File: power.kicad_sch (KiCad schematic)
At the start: 22 parts, among them U19 AP62301_TSOT, U20 AP62301_TSOT

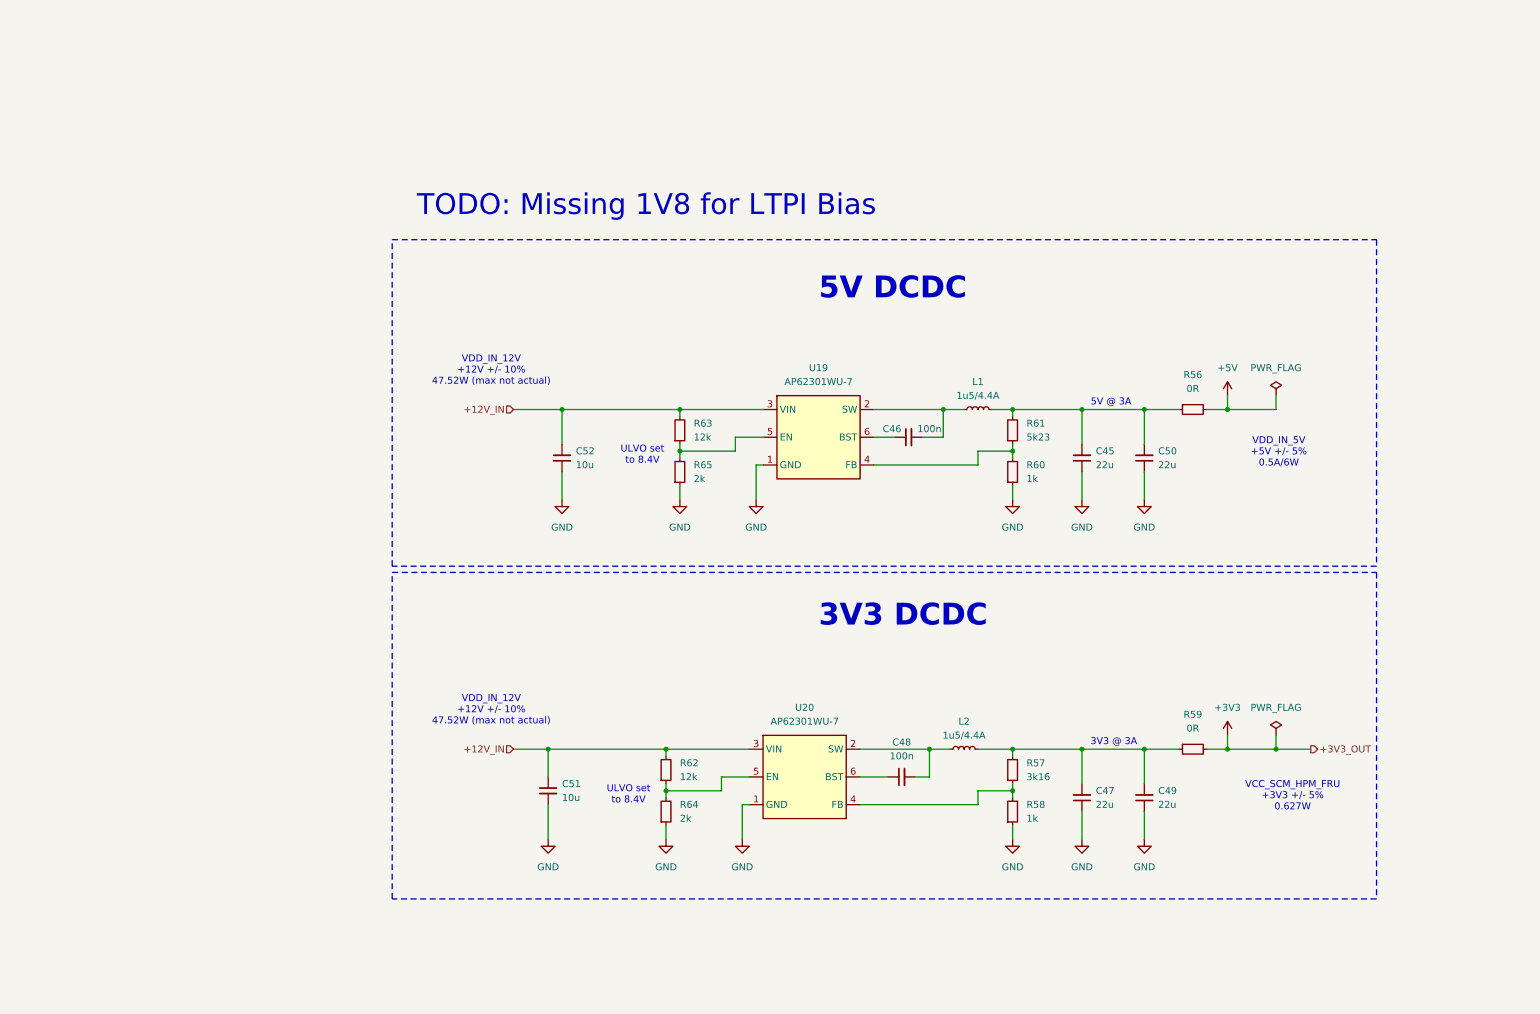
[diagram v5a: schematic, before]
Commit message: [#83363] Replaced 1V8 LDO with DC/DC and moved it to power sheet
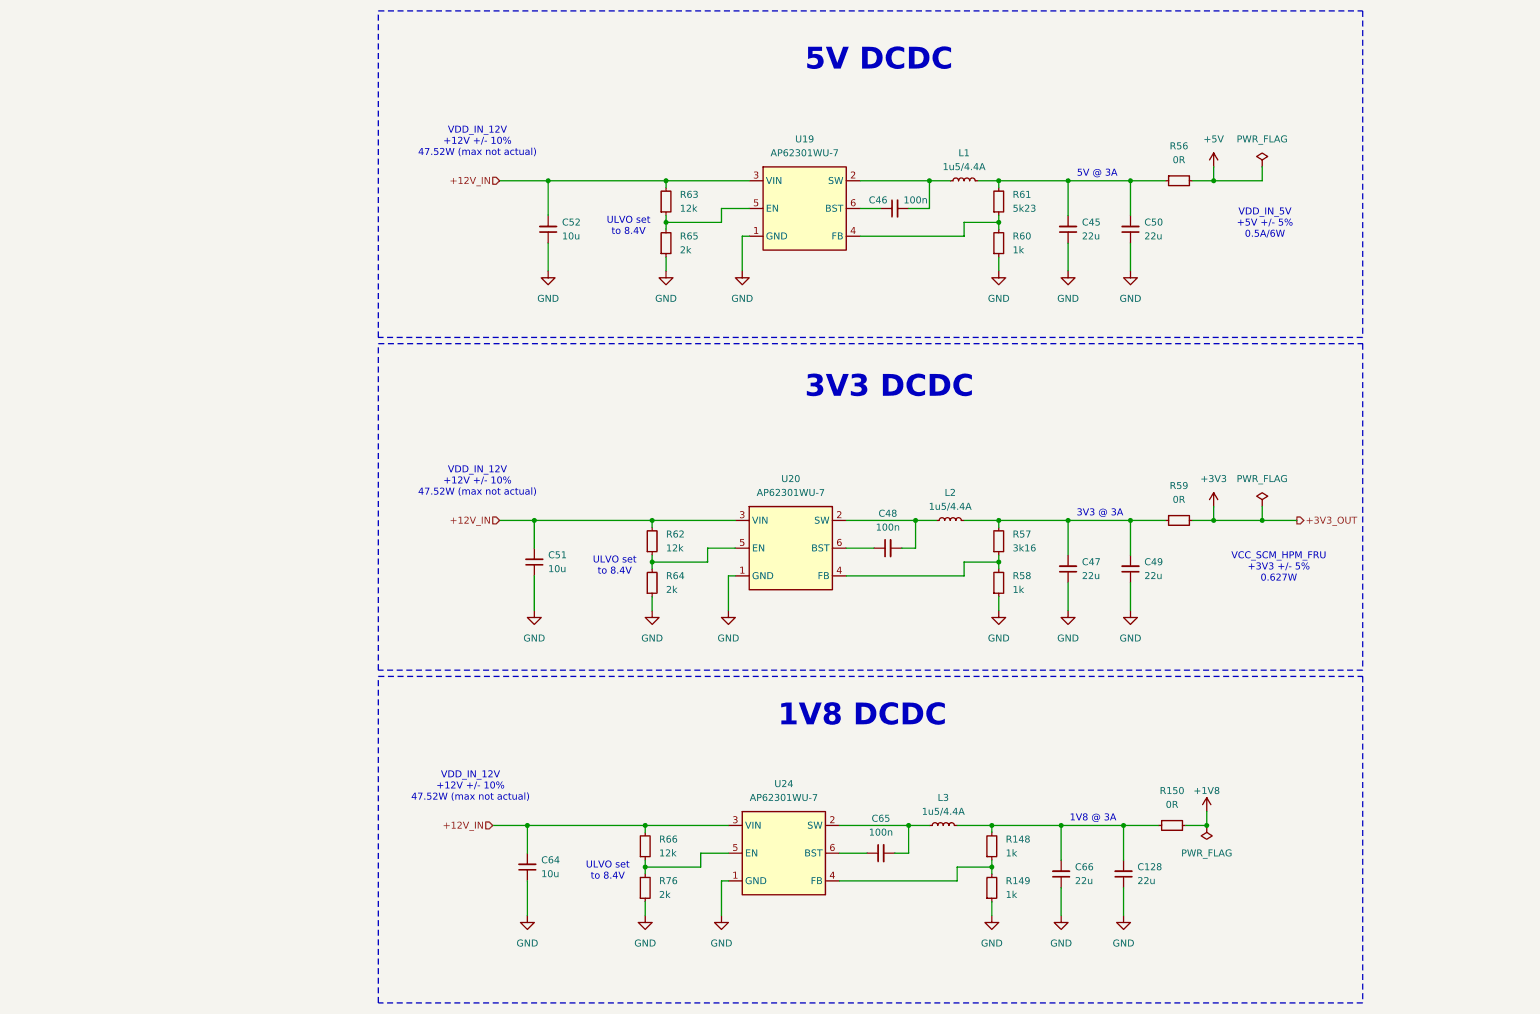
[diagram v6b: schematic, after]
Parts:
- added C128, C66: C_22u_0805_16V, antmicro-footprints:C_0805_2012Metric, symbol antmicroCapacitorsmisc:C_22u_0805_16V
- added C64: C_10u_25V_0603, antmicro-footprints:C_0603_1608Metric, symbol antmicroCapacitors0603:C_10u_25V_0603
- added C65: C_100n_0402, antmicro-footprints:C_0402_1005Metric, symbol antmicroCapacitors0402:C_100n_0402
- added L3: L_1u5_4.4A_Bourns-SRP3212A, antmicro-footprints:L_Bourns-SRP3212A, symbol antmicroFixedInductors:L_1u5_4.4A_Bourns-SRP3212A
- added R148, R149: R_1k_0402, antmicro-footprints:R_0402_1005Metric, symbol antmicroResistors0402:R_1k_0402
- added R150: R_0R_0402, antmicro-footprints:R_0402_1005Metric, symbol antmicroResistors0402:R_0R_0402
- added R66: R_12k_0402, antmicro-footprints:R_0402_1005Metric, symbol antmicroResistors0402:R_12k_0402
- added R76: R_2k_0402, antmicro-footprints:R_0402_1005Metric, symbol antmicroResistors0402:R_2k_0402
- added U24: AP62301_TSOT, antmicro-footprints:TSOT23-6, symbol antmicroDCDCConverters:AP62301_TSOT
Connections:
- net +12V_IN: now also C64.2, R66.2, U24.3 (VIN)
- net GND: now also C128.1, C64.1, C66.1, R149.1, R76.1, U24.1 (GND)
- new net: C65.1, U24.6 (BST)
- new net: C65.2, L3.1, U24.2 (SW)
- new net: R148.1, R149.2, U24.4 (FB)
- new net: R66.1, R76.2, U24.5 (EN)
- new net: C128.2, C66.2, L3.2, R148.2, R150.1
- new net +1V8: R150.2
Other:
- note added: "1V8 @ 3A"
- note added: "1V8 DCDC"
- note removed: "TODO: Missing 1V8 for LTPI Bias"
- moved on the sheet: C45, C46, C47, C48, C49, C50, C51, C52, L1, L2, R56, R57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

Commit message: [#83609] Add load switch IC
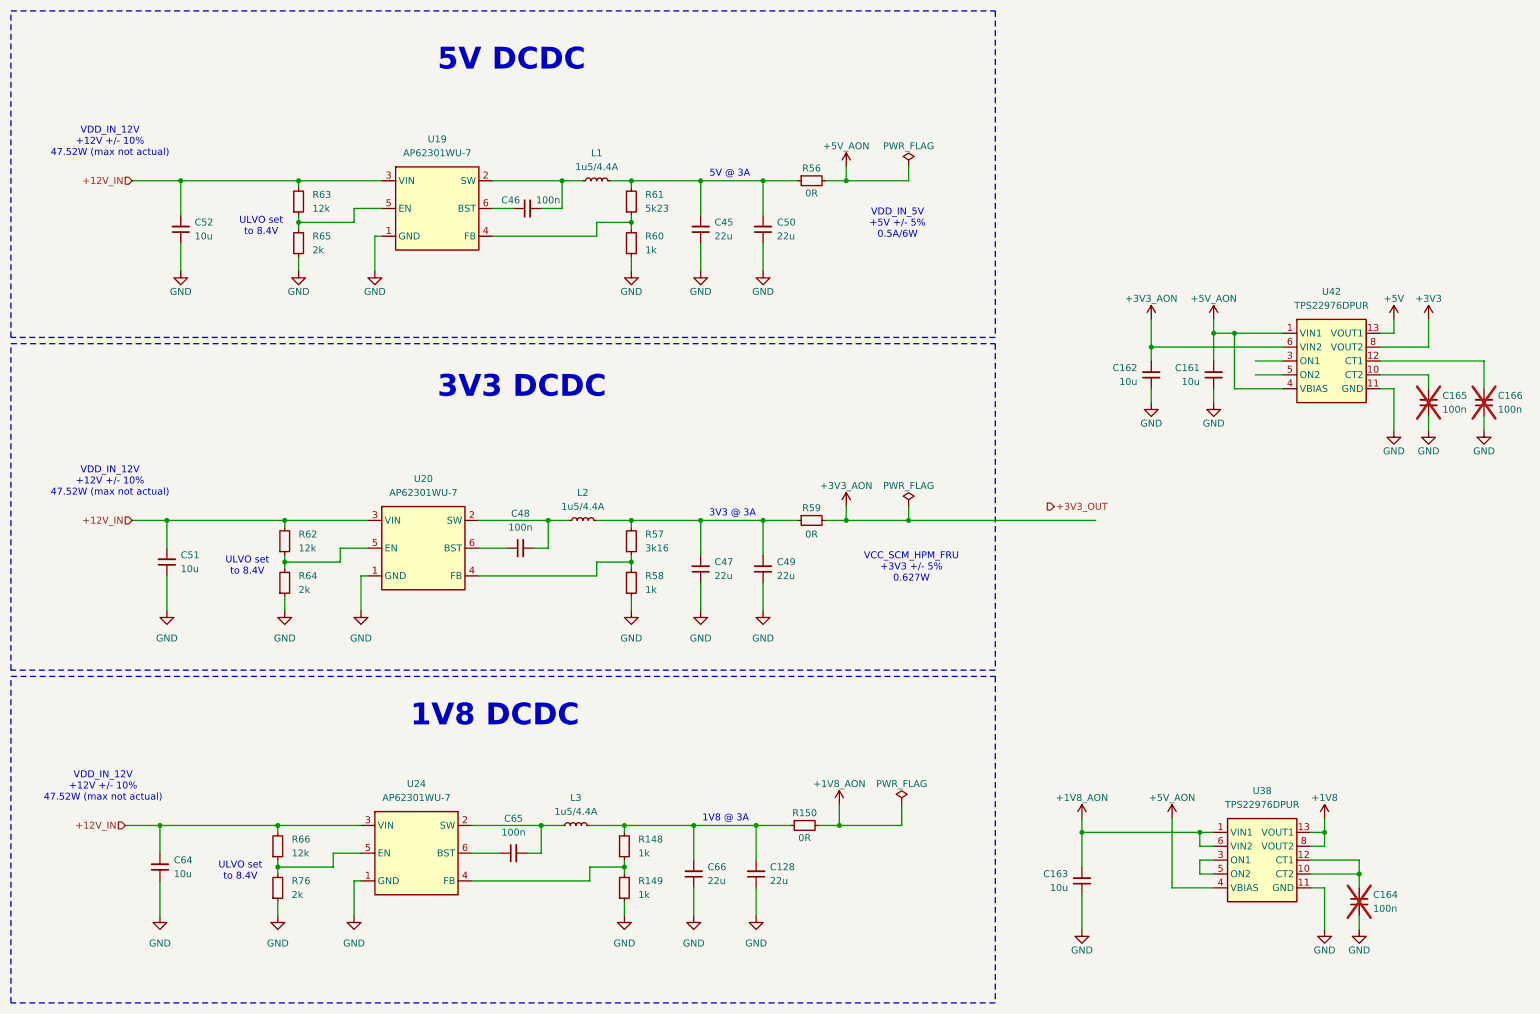
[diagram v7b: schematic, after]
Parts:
- added C161, C162, C163: C_10u_25V_0603, antmicro-footprints:C_0603_1608Metric, symbol antmicroCapacitors0603:C_10u_25V_0603
- added C164, C165, C166: C_100n_0402, antmicro-footprints:C_0402_1005Metric, symbol antmicroCapacitors0402:C_100n_0402
- added U38, U42: TPS22976DPUR, antmicro-footprints:Texas_WSON-14_2x3mm, symbol antmicroPMICPowerDistributionSwitchesLoadDrivers:TPS22976DPUR
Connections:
- net +1V8: now also U38.13 (VOUT1), U38.14 (VOUT1), U38.8 (VOUT2), U38.9 (VOUT2); no longer R150.2
- net +3V3: now also U42.8 (VOUT2), U42.9 (VOUT2); no longer R59.2
- net +5V: now also U42.13 (VOUT1), U42.14 (VOUT1); no longer R56.2
- net GND: now also C161.1, C162.1, C163.1, C164.1, C165.1, C166.1, U38.11 (GND), U38.EP (GND), U42.11 (GND), U42.EP (GND)
- new net: C164.2, U38.10 (CT2), U38.12 (CT1)
- new net: C166.2, U42.12 (CT1)
- new net: C165.2, U42.10 (CT2)
- new net: U38.3 (ON1), U38.5 (ON2)
- new net +1V8_AON: C163.2, R150.2, U38.1 (VIN1), U38.2 (VIN1), U38.6 (VIN2), U38.7 (VIN2)
- new net +3V3_AON: C162.2, R59.2, U42.6 (VIN2), U42.7 (VIN2)
- new net +5V_AON: C161.2, R56.2, U38.4 (VBIAS), U42.1 (VIN1), U42.2 (VIN1), U42.4 (VBIAS)
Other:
- moved on the sheet: C128, C45, C46, C47, C48, C49, C50, C51, C52, C64, C65, C66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

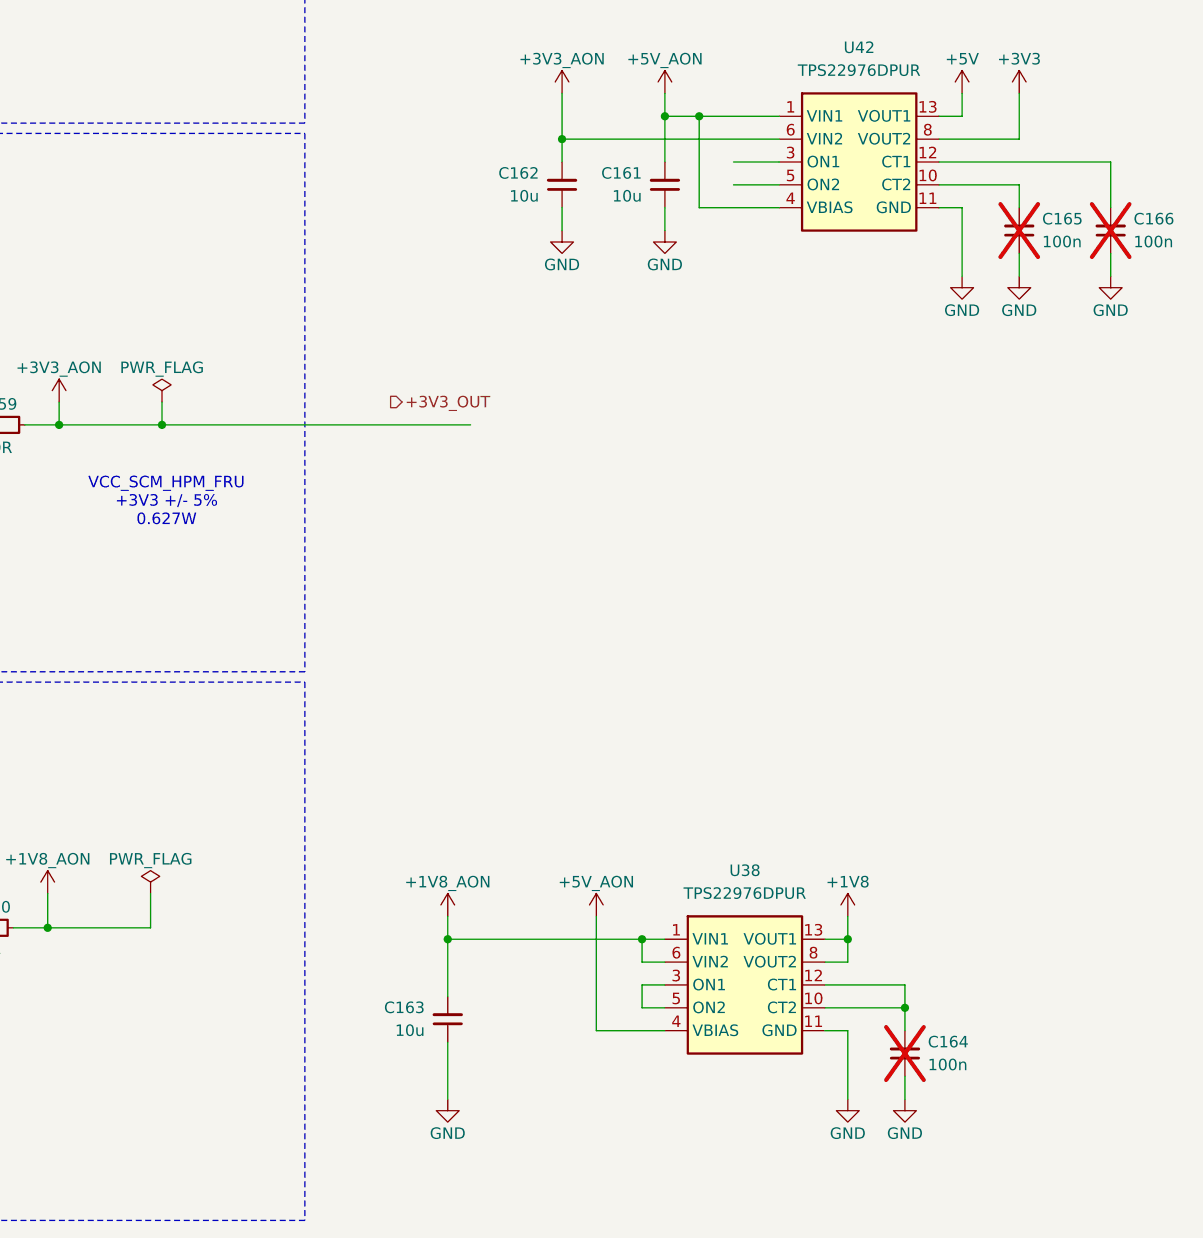
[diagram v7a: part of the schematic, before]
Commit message: [#83609] Add PWR_EN input
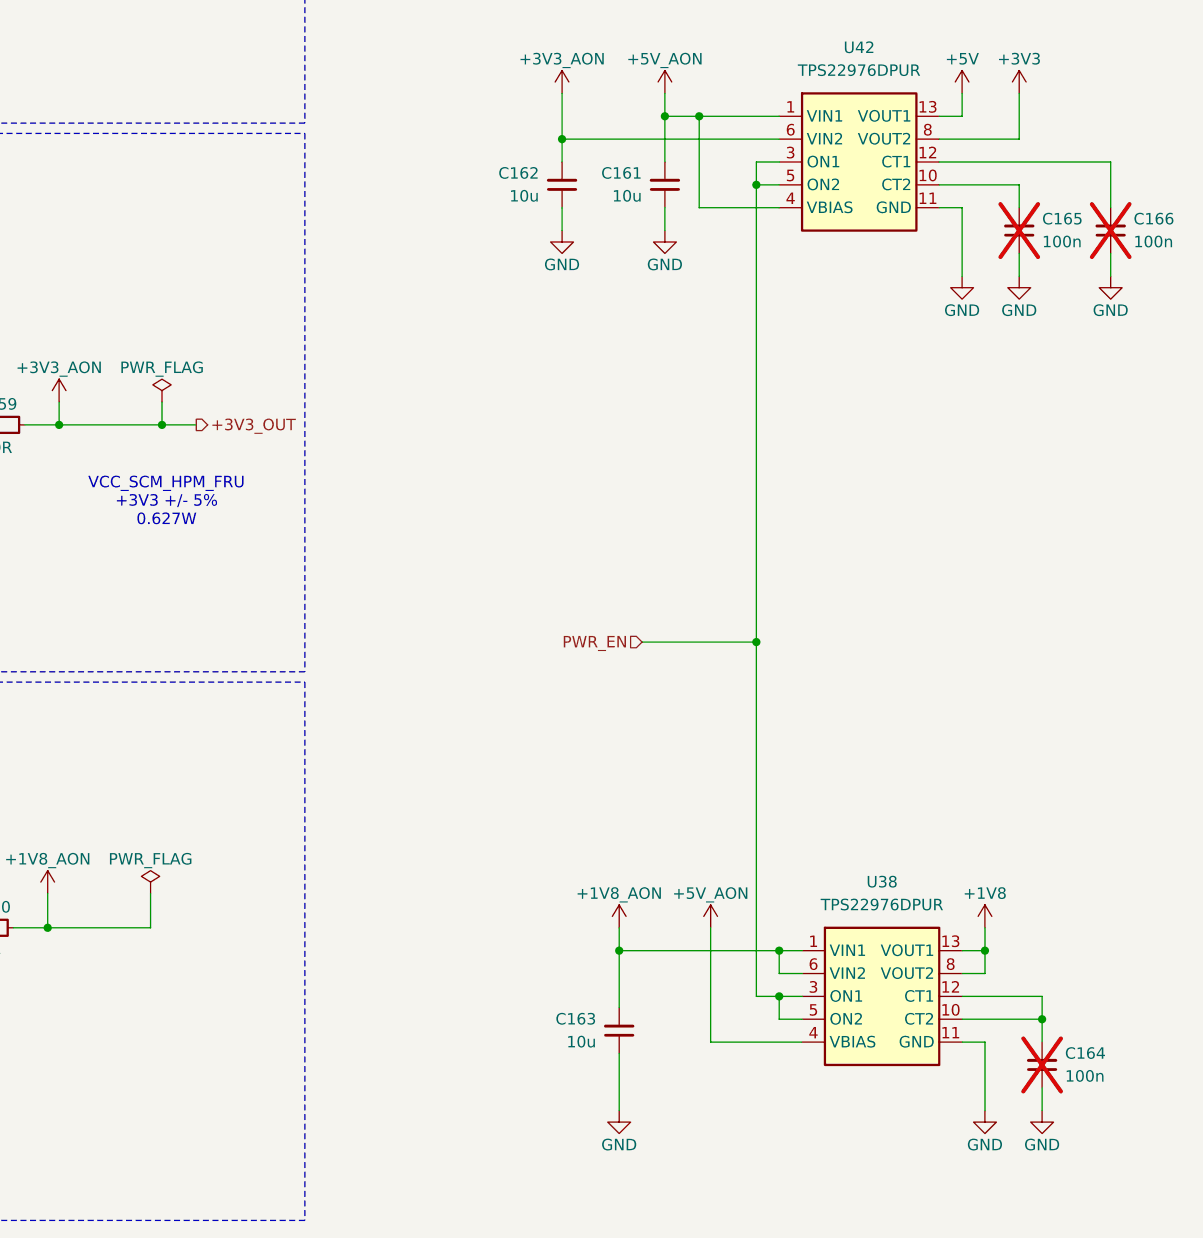
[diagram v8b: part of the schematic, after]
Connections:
- net PWR_EN: now reaches U42.3 (ON1)
- net PWR_EN: now also U38.3 (ON1), U38.5 (ON2), U42.5 (ON2)
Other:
- moved on the sheet: C163, C164, U38
